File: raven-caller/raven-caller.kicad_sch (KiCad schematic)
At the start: 13 parts, among them J1 I2C LCD, Q1 BSS138, SW1 RotaryEncoder_Switch, U1 SeeeduinoXIAO, U2 RFM95W-915S2, U3 24LC256, U4 PCF8574AP

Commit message: schematic v1 done
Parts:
- added C1: 10n, Capacitor_SMD:C_0603_1608Metric, symbol Device:C
- added C2: 4n7, Capacitor_SMD:C_0603_1608Metric, symbol Device:C
- added C29, C3: 3, Capacitor_SMD:C_0603_1608Metric, symbol Device:C
- added C4: 10u, Capacitor_SMD:C_0603_1608Metric, symbol Device:C
- added D2: PMEG6020ER, Diode_SMD:Nexperia_CFP3_SOD-123W, symbol Diode:PMEG6020ER
- added D3, D4: LED, LED_SMD:LED_0603_1608Metric, symbol Device:LED
- added J2: Conn_01x02_Pin, Connector_JST:JST_PH_B2B-PH-K_1x02_P2.00mm_Vertical, symbol Connector:Screw_Terminal_01x02
- added J7: USB_C_Receptacle_USB2.0_16P, Connector_USB:USB_C_Receptacle_GCT_USB4105-xx-A_16P_TopMnt_Horizontal, symbol Connector:USB_C_Receptacle_USB2.0_16P
- added R15, R16: 5k1, Resistor_SMD:R_0603_1608Metric, symbol Device:R
- added R2: 2k, Resistor_SMD:R_0603_1608Metric, symbol Device:R
- added R3, R4, R5: 1k, Resistor_SMD:R_0603_1608Metric, symbol Device:R
- added R6: 100, Resistor_SMD:R_0603_1608Metric, symbol Device:R
- added SW2: SW_DPDT_x2, symbol Switch:SW_DPDT_x2
- added U10, U8, U9: TPD1E05U06DYA, Diode_SMD:D_SOD-523, symbol Power_Protection:TPD1E05U06DYA
- added U5: DW01A, Package_TO_SOT_SMD:SOT-23-6, symbol Battery_Management:DW01A
- added U6: TP4056-42-ESOP8, Package_SO:SOIC-8-1EP_3.9x4.9mm_P1.27mm_EP2.41x3.3mm_ThermalVias, symbol Battery_Management:TP4056-42-ESOP8
- added U7: ~, Package_TO_SOT_SMD:SOT-23-6, symbol FS8205:FS8205
- J1: footprint (none) -> Connector_PinHeader_2.54mm:PinHeader_1x04_P2.54mm_Horizontal
- SW1: footprint (none) -> Rotary_Encoder:RotaryEncoder_Alps_EC11E-Switch_Vertical_H20mm
- U1: footprint (none) -> Xiao Seeed SAMD21:XiaoSeeed
- U3: footprint (none) -> Package_SO:SOIC-8_3.9x4.9mm_P1.27mm
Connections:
- net +3.3V: now also SW1.S1, U1.12 (3V3)
- net 2B: now also U4.6 (P2)
- net 2G: now also U4.5 (P1)
- net 2R: now also U4.4 (P0)
- net BUZZER: now also U1.1 (PA02_A0_D0)
- net GND: now also J1.1 (Pin_1), U1.13 (GND), U2.1 (GND), U2.10 (GND), U2.8 (GND), U3.1 (A0), U3.2 (A1), U3.3 (A2), U3.4 (GND), U4.1 (A0), U4.2 (A1), U4.3 (A2), U4.8 (GND), C1.2, C2.1, C29.1, C3.2, C4.2, J2.2 (Pin_2), J7.A1 (GND), J7.A12 (GND), J7.B1 (GND), J7.B12 (GND), R15.1, R16.2, R2.2, R5.2, U10.2 (GND), U5.6 (GND), U6.1 (TEMP), U6.3 (GND), U7.1 (S1), U7.3 (S2), U8.2 (GND), U9.2 (GND)
- net SDA: now reaches U3.5 (SDA)
- net SDA: now also J1.3 (Pin_3), U1.5 (PA8_A4_D4_SDA), U4.15 (SDA)
- net SCL: now reaches U3.6 (SCL)
- net SCL: now also J1.4 (Pin_4), U1.6 (PA9_A5_D5_SCL), U4.14 (SCL)
- net RotA: now reaches SW1.A
- net RotA: now also U1.2 (PA4_A1_D1)
- net RotC: now reaches SW1.B
- net RotC: now also U1.4 (PA11_A3_D3)
- net RotB: now reaches SW1.C
- net RotB: now also U1.3 (PA10_A2_D2)
- net RotSwit: now reaches SW1.S2
- new net: U5.3 (OC), U7.4 (G2)
- new net: U5.1 (OD), U7.6 (G1)
- new net: C2.2, C29.2, D2.2 (A), D3.2 (A), D4.2 (A), J7.A4 (VBUS), J7.A9 (VBUS), J7.B4 (VBUS), J7.B9 (VBUS), U10.1 (I/O), U6.4 (V_{CC}), U6.8 (CE)
- new net: C3.1, R6.1, U5.5 (VCC)
- new net: C4.1, J2.1 (Pin_1), R6.2, SW2.2 (B), U6.5 (BAT)
- new net: J7.A5 (CC1), R15.2, U8.1 (I/O)
- new net: D3.1 (K), R3.2
- new net: R3.1, U6.7 (~{CHRG})
- new net: R5.1, U5.2 (CS)
- new net: D4.1 (K), R4.2
- new net: R4.1, U6.6 (~{STDBY})
- new net: J7.B5 (CC2), R16.1, U9.1 (I/O)
- new net: C1.1, J7.S1 (SHIELD)
- new net: R2.1, U6.2 (PROG)
- new net +5V: D2.1 (K)
- no-connect marks 0 -> 2
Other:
- moved on the sheet: BZ2, J1, Q1, R1, R13, R18, R19, SW1, U1, U2, U3, U4

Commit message: traces v1 done!
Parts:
- removed SW2: SW_DPDT_x2, symbol Switch:SW_DPDT_x2
- added C5: 4u7, Capacitor_SMD:C_0603_1608Metric, symbol Device:C
- added C6: 10u, Capacitor_SMD:C_0603_1608Metric, symbol Device:C
- added J3: Conn_Coaxial, Connector_Coaxial:U.FL_Molex_MCRF_73412-0110_Vertical, symbol Connector:Conn_Coaxial
- added L1: L, Inductor_SMD:L_6.3x6.3_H3, symbol Device:L
- added R10: 309k, Resistor_SMD:R_0603_1608Metric, symbol Device:R
- added R7, R8: 10k, Resistor_SMD:R_0603_1608Metric, symbol Device:R
- added R9: 976k, Resistor_SMD:R_0603_1608Metric, symbol Device:R
- added SW2: SW_SPDT, Button_Switch_THT:SW_Slide_SPDT_Angled_CK_OS102011MA1Q, symbol Switch:SW_SPDT
- added SW3: SW_Push, Button_Switch_THT:SW_PUSH_6mm, symbol Switch:SW_Push
- added U11: TXS0102DCT, Package_SO:SSOP-8_2.95x2.8mm_P0.65mm, symbol Logic_LevelTranslator:TXS0102DCT
- added U13: MCP1640Cx-xCHY, Package_TO_SOT_SMD:SOT-23-6, symbol Regulator_Switching:MCP1640Cx-xCHY
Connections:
- net +3.3V: now also U2.13 (3.3V), U3.8 (VCC), U4.16 (VDD), C5.1, L1.1, R7.1, R8.2, SW2.1 (A), U11.3 (VCCA), U13.3 (EN), U13.6 (V_{IN})
- net +5V: now also J1.2 (Pin_2), C6.1, R9.1, U11.7 (VCCB), U13.5 (V_{OUT})
- net GND: now also U1.16 (GND), U1.20 (GND), C5.2, C6.2, J3.2 (Ext), R10.2, SW3.2, U11.2 (GND), U13.2 (GND)
- net RotA: now also U4.7 (P3); no longer U1.2 (PA4_A1_D1)
- net RotB: now also U4.9 (P4); no longer U1.3 (PA10_A2_D2)
- net RotC: now also U4.10 (P5); no longer U1.4 (PA11_A3_D3)
- net RotSwit: now also U4.11 (P6)
- net SCL: now also U11.5 (A1); no longer J1.4 (Pin_4)
- net SDA: now also U11.4 (A2); no longer J1.3 (Pin_3)
- net at U7.2 (D1): now also U7.5 (D2)
- net vbus: now reaches C2.2, C29.2, D2.2 (A), D3.2 (A), D4.2 (A), J7.A4 (VBUS), J7.A9 (VBUS), J7.B4 (VBUS), J7.B9 (VBUS), U10.1 (I/O), U6.4 (V_{CC}), U6.8 (CE)
- net Bat: now reaches C4.1, J2.1 (Pin_1), R6.2, U6.5 (BAT)
- net Bat: now also SW2.2 (B)
- net INT: now reaches U2.14 (DIO0)
- net INT: now also U1.3 (PA10_A2_D2)
- net MISO: now reaches U2.2 (MISO)
- net MISO: now also U1.11 (PA6_A10_D10_MOSI)
- net MOSI: now reaches U2.3 (MOSI)
- net MOSI: now also U1.10 (PA5_A9_D9_MISO)
- net SCK: now reaches U2.4 (SCK)
- net SCK: now also U1.9 (PA7_A8_D8_SCK)
- net CS: now reaches U2.5 (NSS)
- net CS: now also U1.2 (PA4_A1_D1), R8.1
- net at U2.9 (ANT): now also J3.1 (In)
- net at U1.19 (RESET): now also SW3.1
- new net: R10.1, R9.2, U13.4 (V_{FB})
- new net: L1.2, U13.1 (SW)
- new net: J1.3 (Pin_3), U11.1 (B2)
- new net: R7.2, U11.6 (OE)
- new net: J1.4 (Pin_4), U11.8 (B1)
- no-connect marks 2 -> 19
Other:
- moved on the sheet: C1, C2, C29, C3, C4, D2, D3, D4, J1, J2, J7, R15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

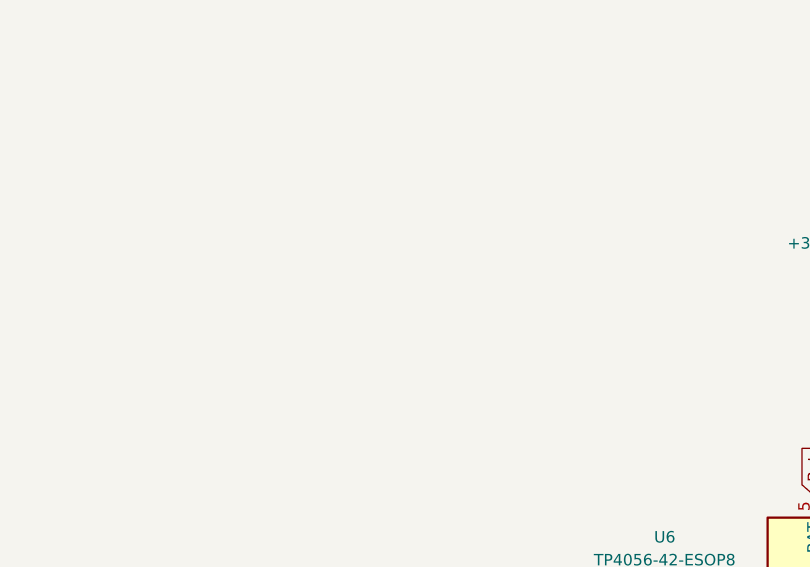
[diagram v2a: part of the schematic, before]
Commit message: routes v2 and "fixed" drc
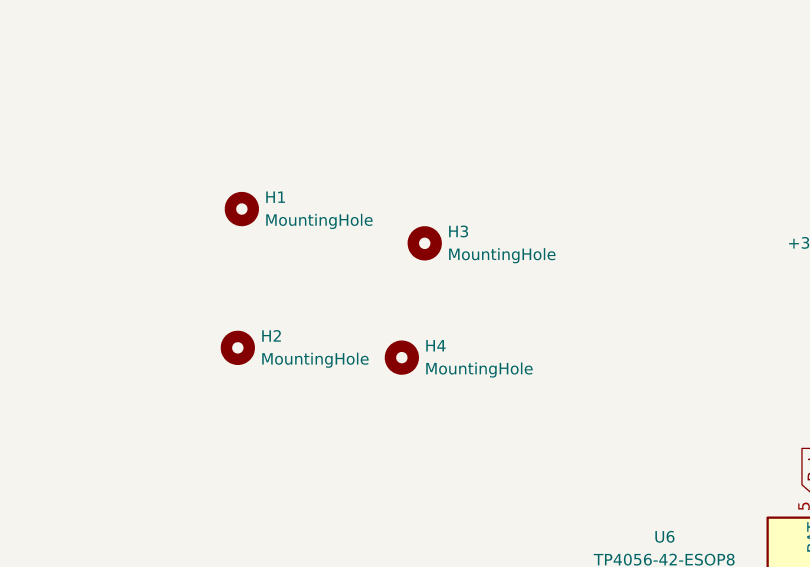
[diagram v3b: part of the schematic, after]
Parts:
- added H1, H2, H3, H4: MountingHole, MountingHole:MountingHole_2.2mm_M2, symbol Mechanical:MountingHole

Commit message: final pcb(i hope)
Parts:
- removed SW3: SW_Push, Button_Switch_THT:SW_PUSH_6mm, symbol Switch:SW_Push
- removed U1: SeeeduinoXIAO, Xiao Seeed SAMD21:XiaoSeeed, symbol Seeeduino XIAO:SeeeduinoXIAO
- added U12: XIAO-SAMD21-DIP, SEEED Xiao:XIAO-SAMD21-DIP, symbol Seeed_Studio_XIAO_Series:XIAO-SAMD21-DIP
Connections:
- net +5V: now also U12.14 (5V)
- net BUZZER: now also U12.1 (PA02_A0_D0)
- net CS: now also U12.2 (PA4_A1_D1)
- net GND: now also U12.13 (GND)
- net INT: now also U12.3 (PA10_A2_D2)
- net MISO: now also U12.11 (PA6_A10_D10_MOSI)
- net MOSI: now also U12.10 (PA5_A9_D9_MISO)
- net SCK: now also U12.9 (PA7_A8_D8_SCK)
- net SCL: now also U12.6 (PA9_A5_D5_SCL)
- net SDA: now also U12.5 (PA8_A4_D4_SDA)
- no-connect marks 19 -> 16

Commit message: final fixes
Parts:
- L1: value L -> 10uH
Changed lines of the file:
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@@
 			)
 		)
-		(property "Value" "L"
+		(property "Value" "10uH"
 			(at 198.12 57.15 90)
 			(effects
